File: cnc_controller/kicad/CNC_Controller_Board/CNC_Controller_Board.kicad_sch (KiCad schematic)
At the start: 29 parts, among them J1 Conn_01x02_Male, J2 Conn_01x02_Male, J3 Conn_01x02_Male, J4 Conn_01x02_Male, J5 Conn_02x08_Counter_Clockwise, J6 Conn_02x16_Counter_Clockwise, U1 74HC14, U2 PC817, U3 PC817, U4 PC817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

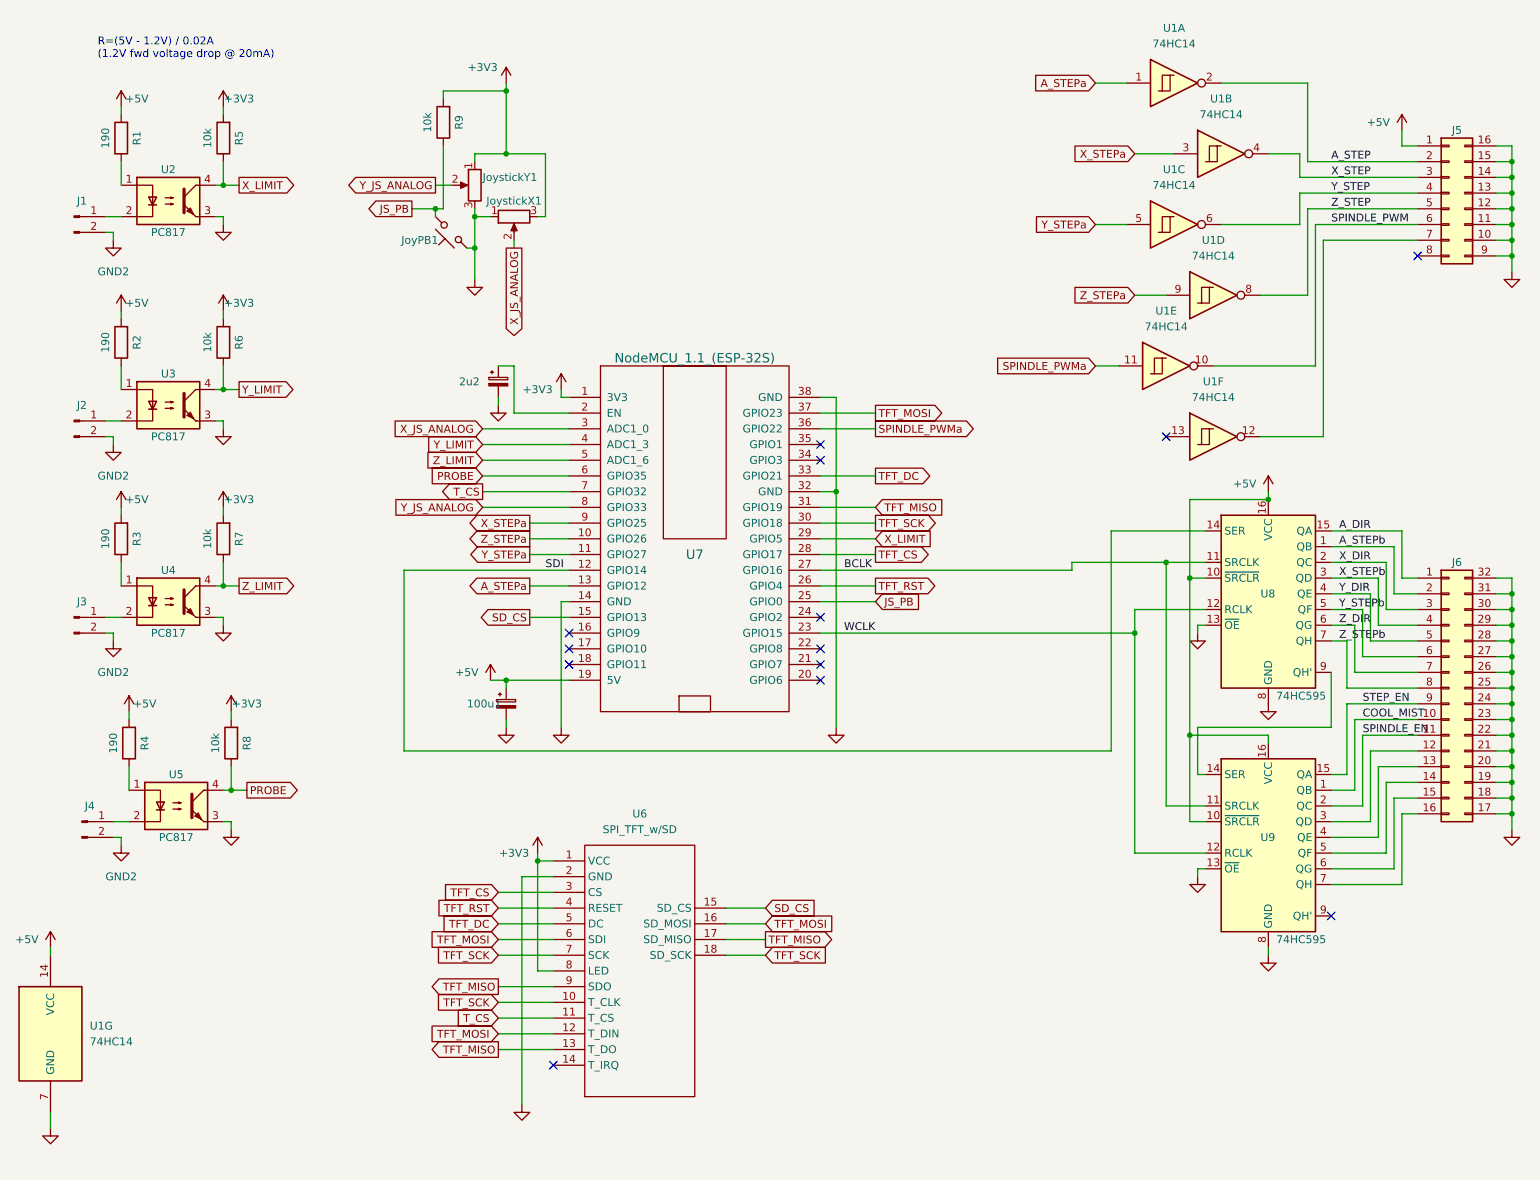
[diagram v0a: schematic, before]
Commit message: CNC Controller: Added OpenSCAD model for prototype enclosure.
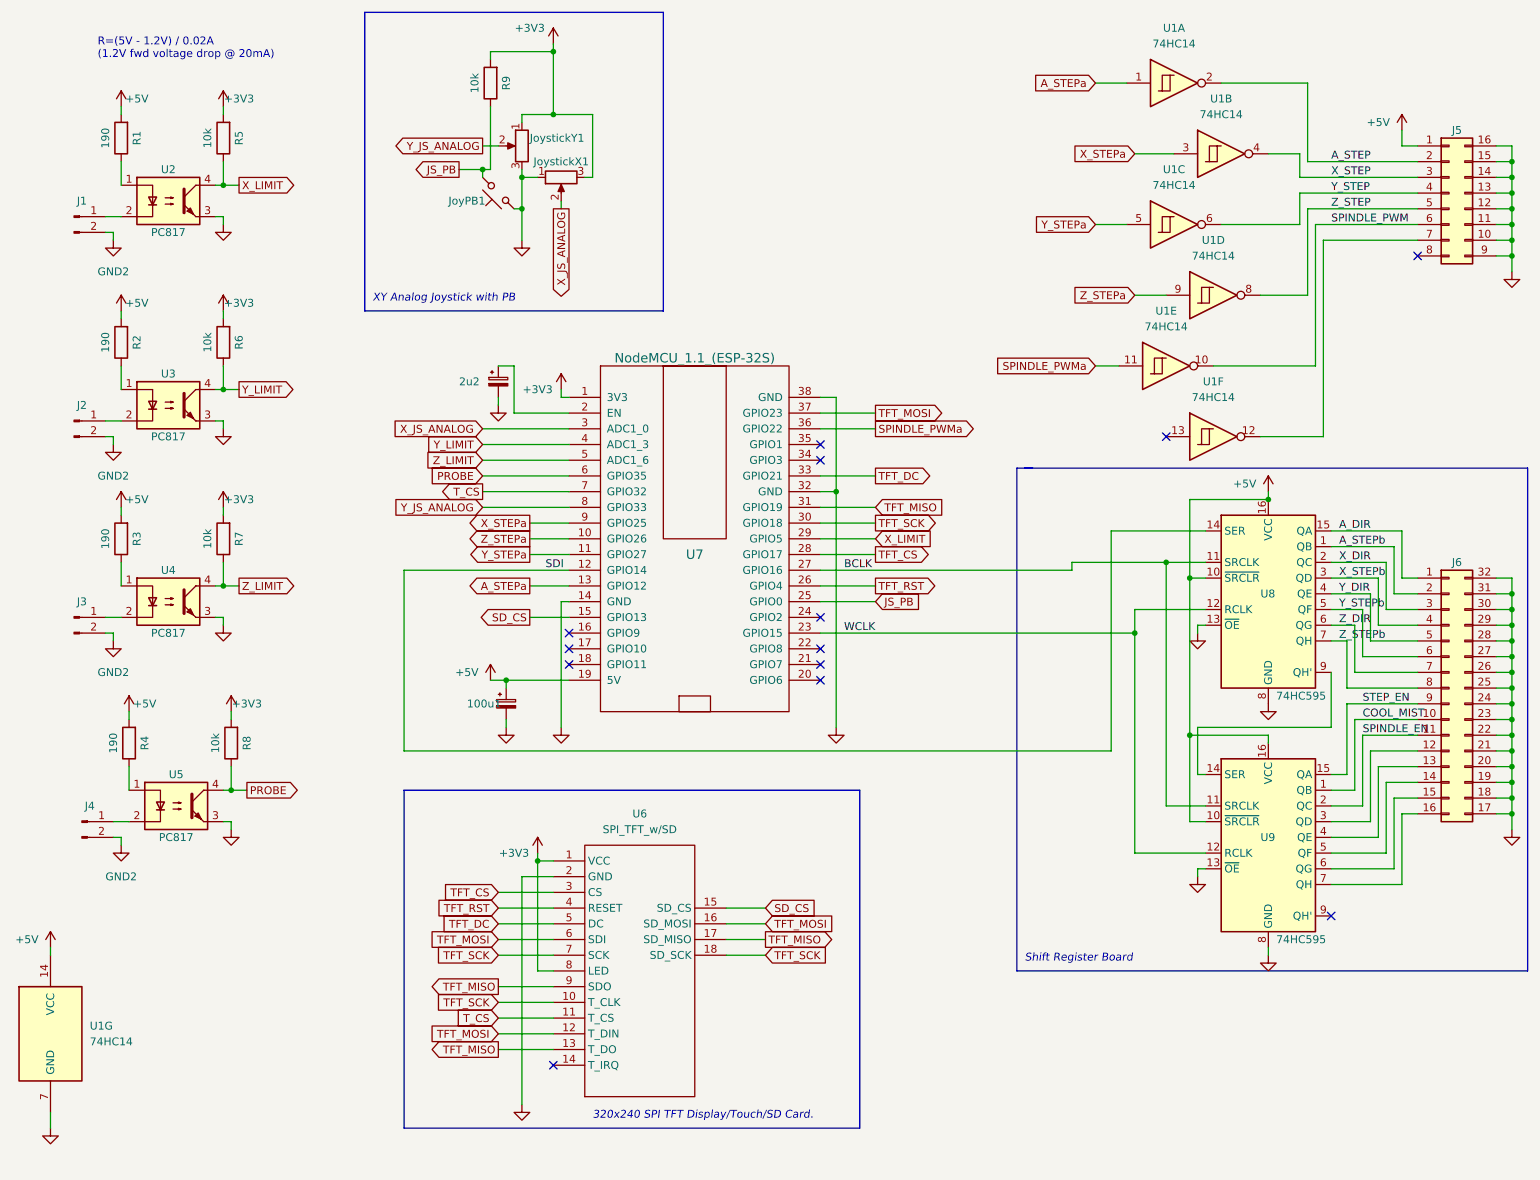
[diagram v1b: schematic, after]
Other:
- note added: "320x240 SPI TFT Display/Touch/SD Card."
- note added: "Shift Register Board"
- note added: "XY Analog Joystick with PB"
- moved on the sheet: JoyPB1, JoystickX1, JoystickY1, R9

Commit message: Updated schematic and pinouts.
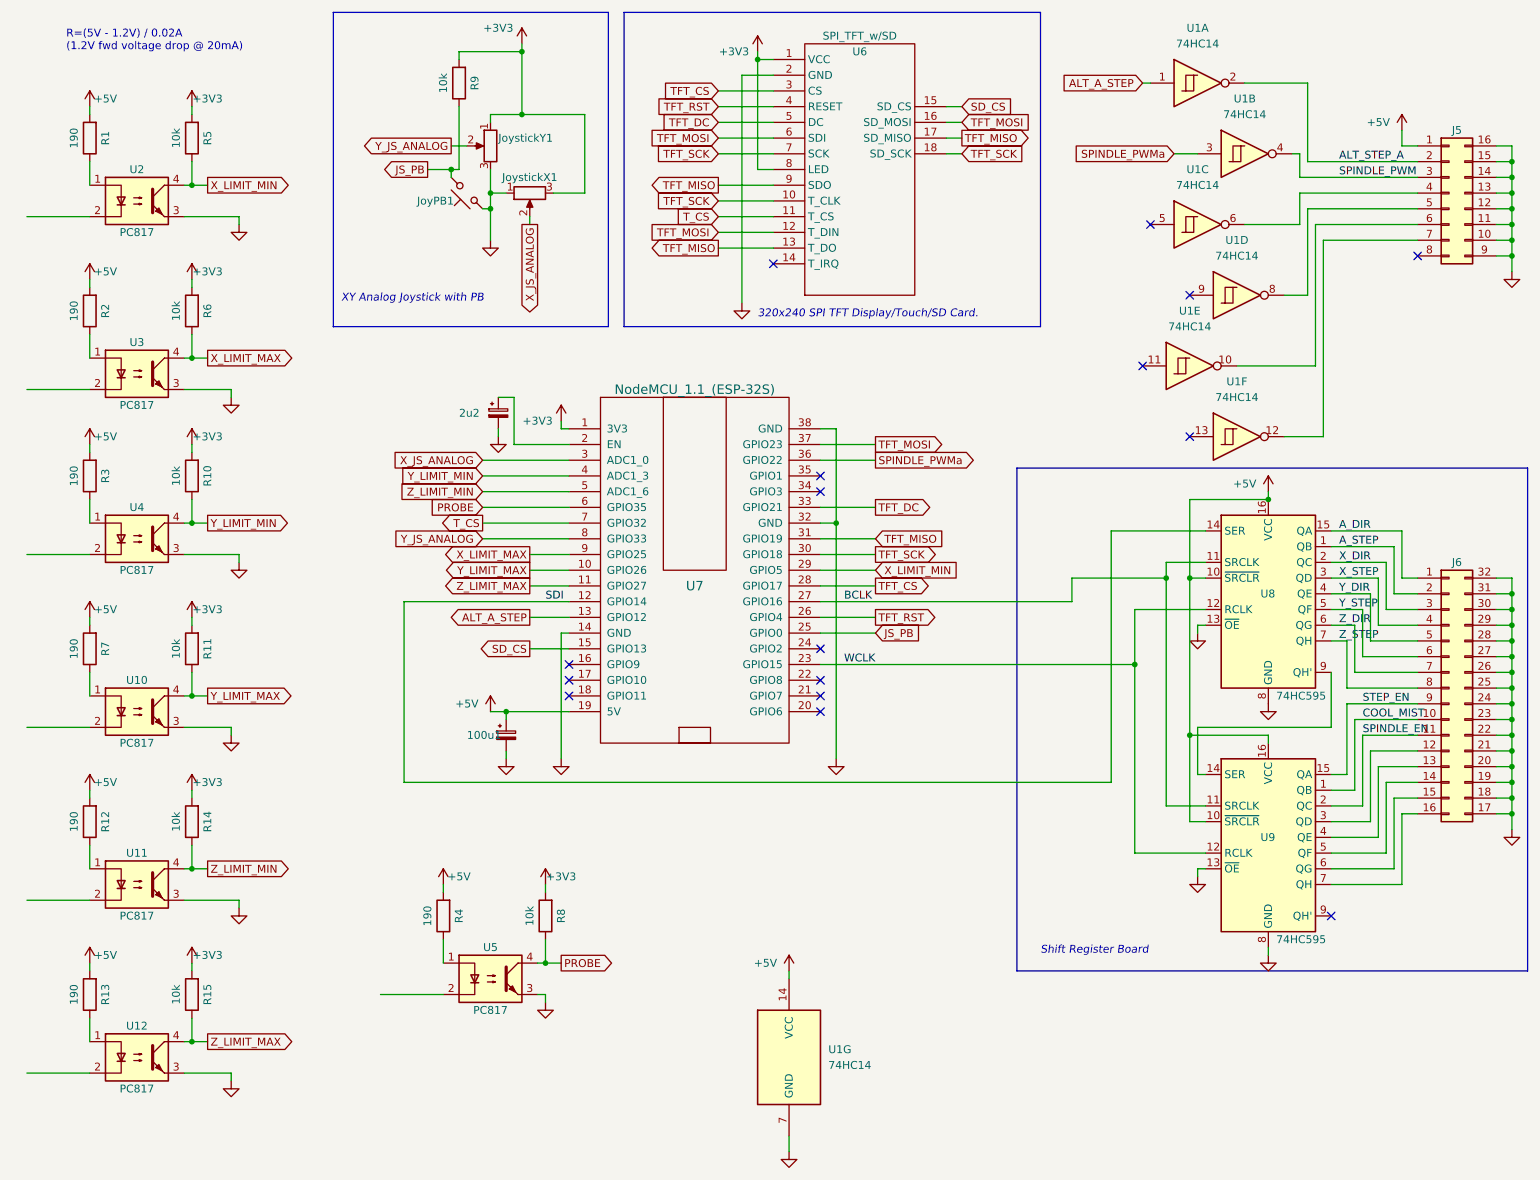
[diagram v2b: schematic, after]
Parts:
- removed J1, J2, J3, J4: Conn_01x02_Male, symbol Connector:Conn_01x02_Male
- added R10, R11, R14, R15: 10k, symbol Device:R
- added R12, R13: 190, symbol Device:R
- added U10, U11, U12: PC817, Package_DIP:DIP-4_W7.62mm, symbol Isolator:PC817
- R7: value 10k -> 190
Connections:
- net A_STEPb is gone; now on net A_STEP: J6.2 (Pin_2), U8.1 (QB)
- net X_STEPb is gone; now on net X_STEP: J6.4 (Pin_4), U8.3 (QD)
- net Y_STEPb is gone; now on net Y_STEP: J6.6 (Pin_6), U8.5 (QF)
- net Z_STEPb is gone; now on net Z_STEP: J6.8 (Pin_8), U8.7 (QH)
- net +3V3: now also R10.2, R11.2, R14.2, R15.2; no longer R7.2
- net +5V: now also R7.2, R12.2, R13.2
- net A_STEP: no longer J5.2 (Pin_2), U1.2
- net GND: now also U10.3, U11.3, U12.3
- net SPINDLE_PWM: now also J5.3 (Pin_3), U1.4; no longer J5.6 (Pin_6), U1.10
- net SPINDLE_PWMa: now also U1.3; no longer U1.11
- net X_STEP: no longer J5.3 (Pin_3), U1.4
- net Y_STEP: no longer J5.4 (Pin_4), U1.6
- net Z_STEP: no longer J5.5 (Pin_5), U1.8
- net A_STEPa renamed ALT_A_STEP
- net X_LIMIT renamed X_LIMIT_MIN
- net X_STEPa renamed X_LIMIT_MAX
- net X_LIMIT_MAX: now also R6.1, U3.4; no longer U1.3
- removed net Y_LIMIT: R6.1, U3.4, U7.4 (ADC1_3)
- net Y_STEPa: no longer names the net of U1.5
- net Y_STEPa: no longer U7.11 (GPIO27)
- removed net Z_LIMIT: R7.1, U4.4, U7.5 (ADC1_6)
- net Z_STEPa: no longer names the net of U1.9
- net Z_STEPa: no longer U7.10 (GPIO26)
- new net: J5.4 (Pin_4), U1.6
- new net: J5.5 (Pin_5), U1.8
- new net: J5.6 (Pin_6), U1.10
- new net: R13.1, U12.1
- new net: R7.1, U10.1
- new net: R12.1, U11.1
- new net ALT_STEP_A: J5.2 (Pin_2), U1.2
- new net Y_LIMIT_MAX: R11.1, U10.4, U7.10 (GPIO26)
- new net Y_LIMIT_MIN: R10.1, U4.4, U7.4 (ADC1_3)
- new net Z_LIMIT_MAX: R15.1, U12.4, U7.11 (GPIO27)
- new net Z_LIMIT_MIN: R14.1, U11.4, U7.5 (ADC1_6)
- no-connect marks 13 -> 16
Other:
- moved on the sheet: 100u1, 2u2, JoyPB1, JoystickX1, JoystickY1, R1, R2, R4, R5, R6, R8, R9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
